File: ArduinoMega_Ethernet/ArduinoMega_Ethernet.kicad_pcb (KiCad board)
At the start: 2 copper layers, 101.6 x 53.3 mm, 113 parts, among them J1 RJ45_Amphenol_RJMG1BD3B8K1ANR, J11 Micro_SD_Card_Det_Hirose_DM3AT, J2 SD_DET_JUMP, J3 IMU_INT1_JUMP, J4 IMU_INT2_JUMP, J5 ETHER_INT_JUMP, J6 RTC_MFP_JUMP, J9 PROGRAM_POWER_USBC, SW1 RST_BTN, U1 ATmega2560-16A, U2 CH340C, U3 ISM330DHCX, U4 W5500, U5 LM3281, U6 74HC244, U7 SE050C2HQ1, U8 AP22804AW5, U9 MCP7940N-xST, Y1 16Mhz, Y2 25Mhz, Y3 Crystal_GND23

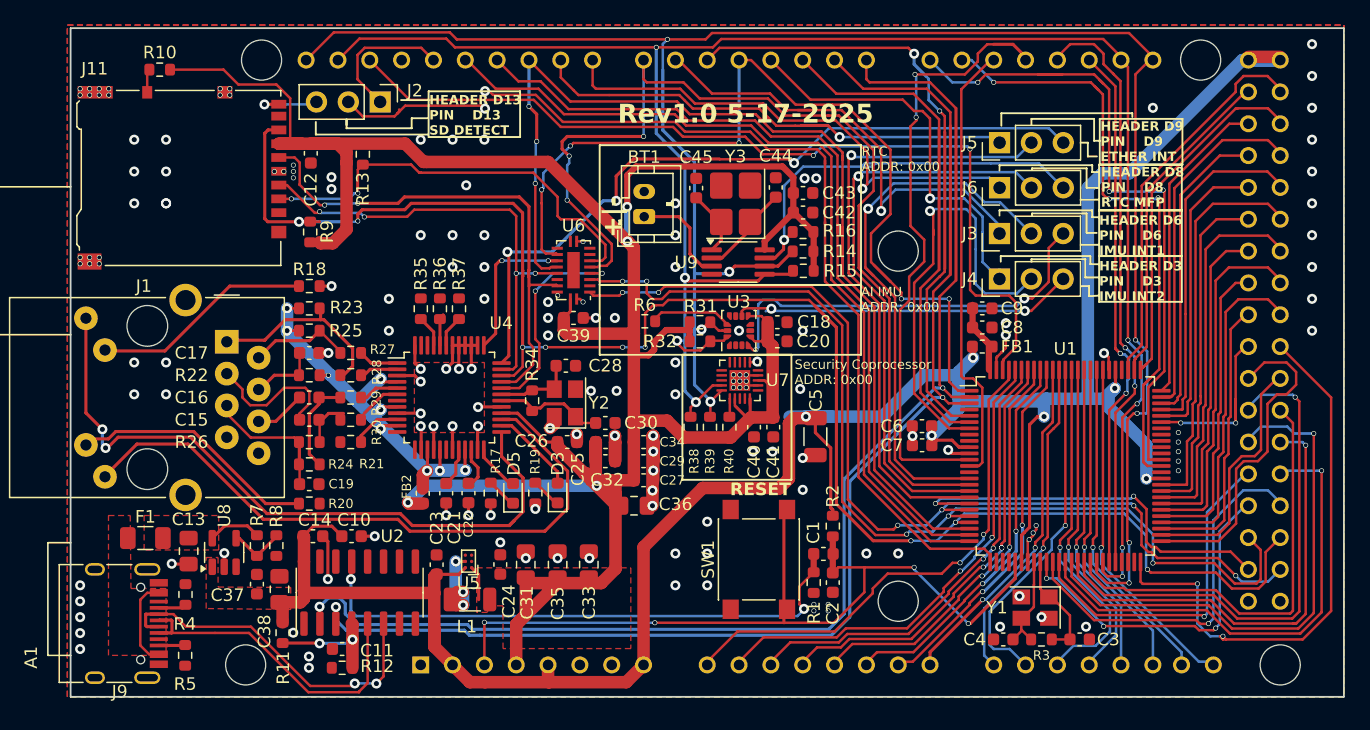
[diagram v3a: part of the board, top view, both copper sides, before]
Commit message: I2C and Silkscreen revision
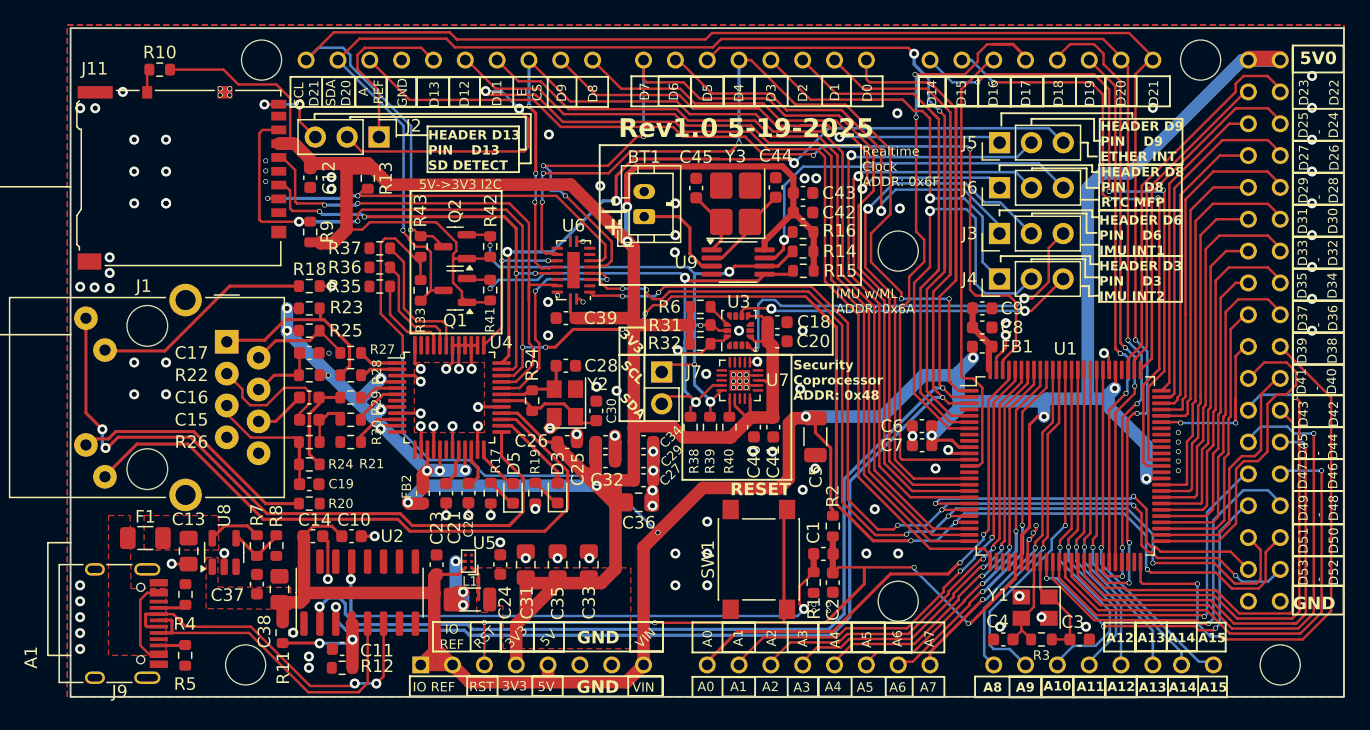
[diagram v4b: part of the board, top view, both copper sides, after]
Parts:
- added J7: EXT_3V3_I2C, Connector_PinHeader_2.54mm:PinHeader_1x02_P2.54mm_Vertical, F.Cu at (90.3, 155.7)
- added Q1: BSS138, Package_TO_SOT_SMD:SOT-23, F.Cu at (73.9, 149.2)
- added Q2: BSS138, Package_TO_SOT_SMD:SOT-23, F.Cu at (73.9, 145.7)
- added R33: 10k, Resistor_SMD:R_0603_1608Metric, F.Cu at (71.1, 149.2)
- added R41: 10k, Resistor_SMD:R_0603_1608Metric, F.Cu at (76.7, 149.2)
- added R42: 10k, Resistor_SMD:R_0603_1608Metric, F.Cu at (76.7, 145.7)
- added R43: 10k, Resistor_SMD:R_0603_1608Metric, F.Cu at (71.1, 145.7)
- moved R37 7.95 mm to (67.8, 145.8), turned to 0 degrees
- moved R36 5.82 mm to (67.8, 147.3), turned to 0 degrees
- moved R6 4.57 mm to (93.4, 150.5)
- moved R35 3.73 mm to (67.8, 148.9), turned to 0 degrees
- moved J2 2.80 mm to (67.8, 136.9)
- moved R13 1.97 mm to (66.9, 140.2)
- moved C12 1.95 mm to (62.3, 140.2)
- moved C30 1.21 mm to (85.1, 158.8), turned to -90 degrees
- moved C39 0.61 mm to (82.7, 151.4), turned to 0 degrees
- moved C36 0.46 mm to (88.5, 166.1)
- moved R31 0.23 mm to (93.4, 151.9)
- moved R32 0.20 mm to (93.4, 153.4)
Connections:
- A1 pad NC: /IOREF0 -> +5V
- R14 pad 2: /PIN_D21 -> /I2C_SCL_3V3
- R15 pad 2: /PIN_D20 -> /I2C_SDA_3V3
- R31 pad 2: /PIN_D21 -> /I2C_SCL_3V3
- R32 pad 2: /PIN_D20 -> /I2C_SDA_3V3
- R38 pad 2: /PIN_D20 -> /I2C_SDA_3V3
- R39 pad 2: /PIN_D21 -> /I2C_SCL_3V3
- U3 pad 13: /PIN_D21 -> /I2C_SCL_3V3
- U3 pad 14: /PIN_D20 -> /I2C_SDA_3V3
- U7 pad 10: /PIN_D21 -> /I2C_SCL_3V3
- U7 pad 9: /PIN_D20 -> /I2C_SDA_3V3
- U9 pad 5: /PIN_D20 -> /I2C_SDA_3V3
- U9 pad 6: /PIN_D21 -> /I2C_SCL_3V3
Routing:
- net /I2C_SDA_3V3: track 0.00 -> 50.7 mm, vias 0 -> 4
- net +5V: track 205.3 -> 254.3 mm, vias 6 -> 8
- net /I2C_SCL_3V3: track 0.00 -> 48.1 mm, vias 0 -> 5
- net /PIN_D20: track 157.6 -> 134.7 mm, vias 8 -> 5
- net +3V3: track 236.2 -> 257.9 mm
- net /PIN_D21: track 162.8 -> 141.1 mm, vias 8 -> 5
- net /PIN_D13: track 82.8 -> 91.4 mm
- net Net-(U4-PMODE2): track 2.52 -> 10.8 mm
- net GND: track 68.0 -> 60.6 mm, vias 162 -> 142
- net Net-(U4-PMODE1): track 2.48 -> 9.25 mm
- net Net-(U4-PMODE0): track 2.52 -> 7.22 mm
- net Net-(U3-CS): track 6.36 -> 1.93 mm
- net /ETHER_CS: track 86.5 -> 82.4 mm
- net /PIN_D50: track 137.2 -> 140.8 mm
- net /HEAD_D13: track 11.2 -> 14.0 mm
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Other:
- board text added: "3V3"
- board text added: "5V"
- board text added: "5V->3V3 I2C"
- board text added: "5V0"
- board text added: "A REF"
- board text added: "A0"
- board text added: "A1"
- board text added: "A10"
- board text added: "A11"
- board text added: "A12"
- board text added: "A13"
- board text added: "A14"
- board text added: "A15"
- board text added: "A2"
- board text added: "A3"
- board text added: "A4"
- board text added: "A5"
- board text added: "A6"
- board text added: "A7"
- board text added: "A8"
- board text added: "A9"
- board text added: "D0"
- board text added: "D1"
- board text added: "D11"
- board text added: "D12"
- board text added: "D13"
- board text added: "D14"
- board text added: "D15"
- board text added: "D16"
- board text added: "D17"
- board text added: "D18"
- board text added: "D19"
- board text added: "D2"
- board text added: "D20"
- board text added: "D21"
- board text added: "D23 D22"
- board text added: "D25 - D24"
- board text added: "D27 D26"
- board text added: "D29 - D28"
- board text added: "D3"
- board text added: "D31 D30"
- board text added: "D33 - D32"
- board text added: "D35 D34"
- board text added: "D37 - D36"
- board text added: "D39 D38"
- board text added: "D4"
- board text added: "D41 - D40"
- board text added: "D43 D42"
- board text added: "D45 - D44"
- board text added: "D47 D46"
- board text added: "D49 - D48"
- board text added: "D5"
- board text added: "D51 D50"
- board text added: "D53 - D52"
- board text added: "D6"
- board text added: "D7"
- board text added: "D8"
- board text added: "D9"
- board text added: "E CS"
- board text added: "GND"
- board text added: "IMU w/ML ADDR: 0x6A"
- board text added: "IO REF"
- board text added: "RST"
- board text added: "Realtime Clock ADDR: 0x6F"
- board text added: "Rev1.0 5-19-2025"
- board text added: "SCL"
- board text added: "SCL D21"
- board text added: "SDA"
- board text added: "SDA D20"
- board text added: "Security Coprocessor ADDR: 0x48"
- board text added: "VIN"
- board text removed: "AI IMU ADDR: 0x00"
- board text removed: "RTC ADDR: 0x00"
- board text removed: "Rev1.0 5-17-2025"
- board text removed: "Security Coprocessor ADDR: 0x00"

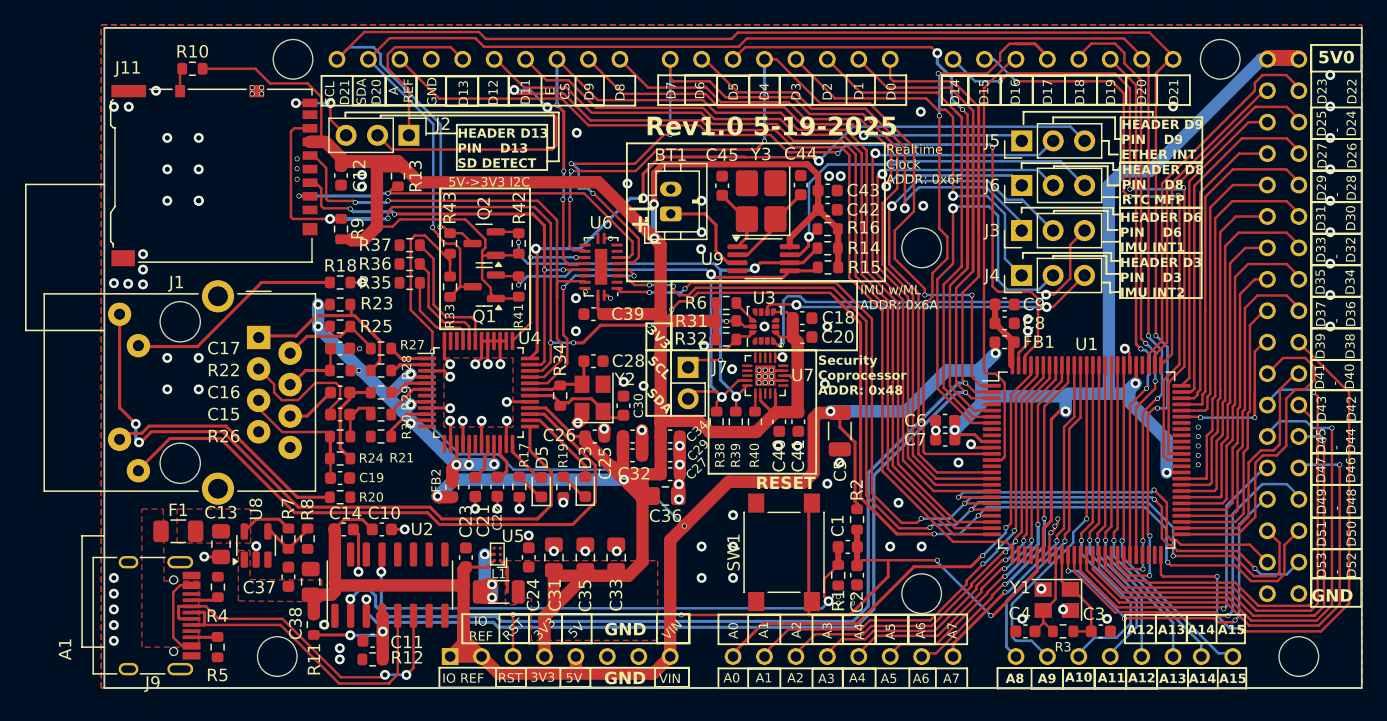
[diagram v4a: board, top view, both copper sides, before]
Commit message: update level shifter, configurable pmode
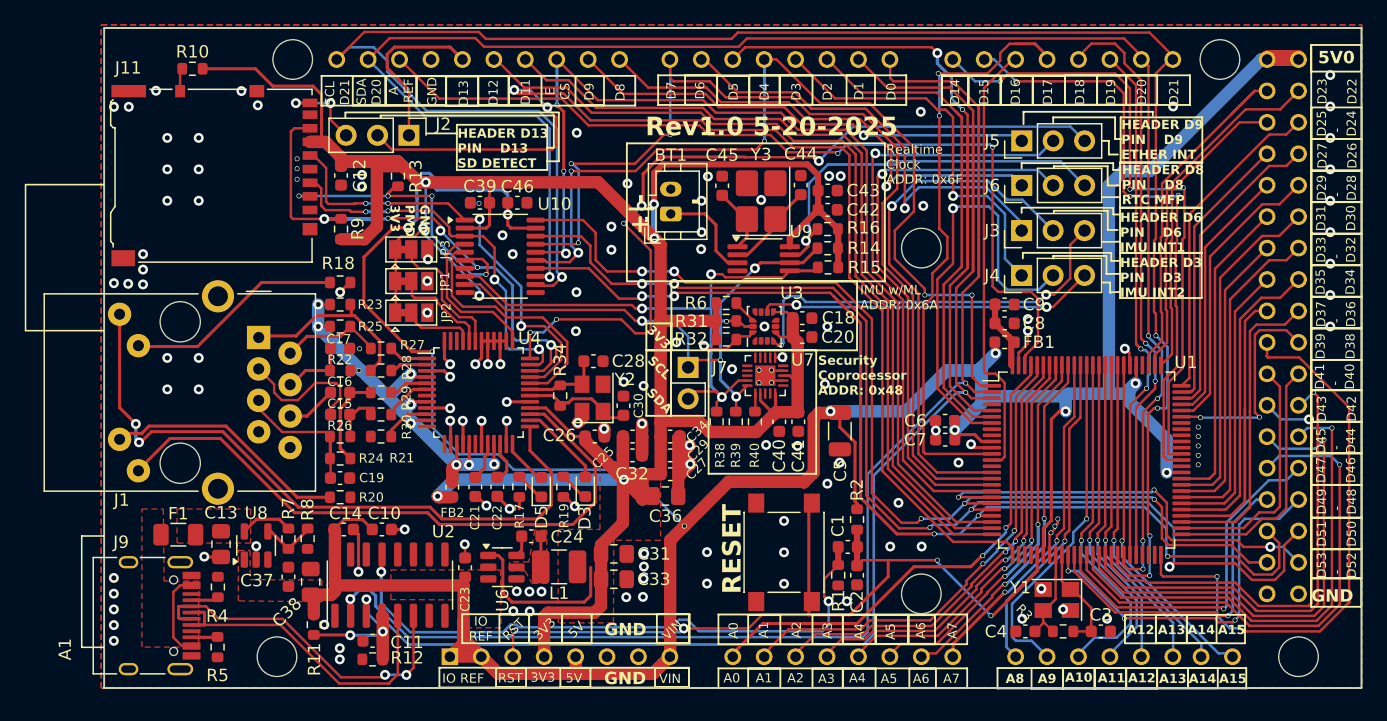
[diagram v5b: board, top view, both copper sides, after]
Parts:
- removed C35: 10uF, Capacitor_SMD:C_0805_2012Metric_Pad1.18x1.45mm_HandSolder
- removed Q1, Q2: BSS138, Package_TO_SOT_SMD:SOT-23
- removed R33, R35, R36, R37, R41, R42, R43: 10k, Resistor_SMD:R_0603_1608Metric
- removed U5: LM3281, Package_BGA:Texas_DSBGA-6_0.9x1.4mm_Layout2x3_P0.5mm
- added C46: 1uF, Capacitor_SMD:C_0603_1608Metric, F.Cu at (76.5, 142.4)
- added JP1: PMODE1, Jumper:SolderJumper-3_P1.3mm_Bridged12_Pad1.0x1.5mm, F.Cu at (68.0, 148.7)
- added JP2: PMODE0, Jumper:SolderJumper-3_P1.3mm_Bridged12_Pad1.0x1.5mm, F.Cu at (68.0, 151.3)
- added JP3: PMODE2, Jumper:SolderJumper-3_P1.3mm_Bridged12_Pad1.0x1.5mm, F.Cu at (68.0, 146.2)
- added U10: TXS0108EPW, Package_SO:TSSOP-20_4.4x6.5mm_P0.65mm, F.Cu at (75.2, 146.7)
- A1: footprint footprints:ARDUINO_A000067 -> CUSTOM_PAD:ARDUINO_A000067
- C20, C34, C39, C41, C43, C6: value 100nF -> 1uF
- C23: value 2.2uF -> 10uF
- C24: value 2.2uF -> 100nF
- C3, C4: value Var -> 22pF
- C31, C33: value 10uF -> 22uF
- L1: value 0.47uH/2A -> 4.7uH; footprint Inductor_SMD:L_1206_3216Metric -> Inductor_SMD:L_1210_3225Metric_Pad1.42x2.65mm_HandSolder
- U6: value 74HC244 -> AP63203WU; footprint Package_DFN_QFN:WQFN-20-1EP_2.5x4.5mm_P0.5mm_EP1x2.9mm -> Package_TO_SOT_SMD:TSOT-23-6
- moved U6 25.6 mm to (75.3, 171.8), turned to 0 degrees
- moved C39 12.9 mm to (73.5, 142.4)
- moved L1 5.28 mm to (79.9, 171.8)
- moved C31 4.86 mm to (84.3, 170.8), turned to 0 degrees
- moved C33 1.77 mm to (84.3, 172.8), turned to 0 degrees
- moved C24 1.72 mm to (77.7, 169.3), turned to 180 degrees
- moved C23 0.81 mm to (72.3, 171.9)
- moved F1 0.28 mm to (49.1, 169.2)
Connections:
- net /I2C_SCL_3V3 renamed /PWRandPRG/IMU_SCL
- net /I2C_SDA_3V3 renamed /PWRandPRG/IMU_SDA
- A1 pad 22: /PIN_D23 -> /PIN_D22
- A1 pad 23: /PIN_D22 -> /PIN_D23
- A1 pad 24: /PIN_D25 -> /PIN_D24
- A1 pad 25: /PIN_D24 -> /PIN_D25
- A1 pad 26: /PIN_D27 -> /PIN_D26
- A1 pad 27: /PIN_D26 -> /PIN_D27
- A1 pad 28: /PIN_D29 -> /PIN_D28
- A1 pad 29: /PIN_D28 -> /PIN_D29
- A1 pad 30: /PIN_D31 -> /PIN_D30
- A1 pad 31: /PIN_D30 -> /PIN_D31
- A1 pad 32: /PIN_D33 -> /PIN_D32
- A1 pad 33: /PIN_D32 -> /PIN_D33
- A1 pad 34: /PIN_D35 -> /PIN_D34
- A1 pad 35: /PIN_D34 -> /PIN_D35
- A1 pad 36: /PIN_D37 -> /PIN_D36
- A1 pad 37: /PIN_D36 -> /PIN_D37
- A1 pad 38: /PIN_D39 -> /PIN_D38
- A1 pad 39: /PIN_D38 -> /PIN_D39
- A1 pad 40: /PIN_D41 -> /PIN_D40
- A1 pad 41: /PIN_D40 -> /PIN_D41
- A1 pad 42: /PIN_D43 -> /PIN_D42
- A1 pad 43: /PIN_D42 -> /PIN_D43
- A1 pad 44: /PIN_D45 -> /PIN_D44
- A1 pad 45: /PIN_D44 -> /PIN_D45
- A1 pad 46: /PIN_D47 -> /PIN_D46
- A1 pad 47: /PIN_D46 -> /PIN_D47
- A1 pad 48: /PIN_D49 -> /PIN_D48
- A1 pad 49: /PIN_D48 -> /PIN_D49
- A1 pad 50: /PIN_D51 -> /PIN_D50
- A1 pad 51: /PIN_D50 -> /PIN_D51
- A1 pad 52: /PIN_D53 -> /PIN_D52
- A1 pad 53: /PIN_D52 -> /PIN_D53
- C24 pad 1: +3V3 -> Net-(U6-SW)
- C24 pad 2: GND -> Net-(U6-BST)
- J11 pad 7: /PIN_D50 -> /PWRandPRG/ETHERNET_MISO
- L1 pad 1: Net-(U5-SW) -> Net-(U6-SW)
- R9 pad 2: /PIN_D50 -> /PWRandPRG/ETHERNET_MISO
- U4 pad 34: /PIN_D50 -> /PWRandPRG/ETHERNET_MISO
- U6 pad 1: GND -> +3V3
- U6 pad 2: /PIN_D52 -> +5V
- U6 pad 3: unconnected-(U6-2Y0-Pad3) -> +5V
- U6 pad 4: /PIN_D51 -> GND
- U6 pad 5: /PWRandPRG/ETHERNET_CS -> Net-(U6-SW)
- U6 pad 6: /ETHER_~{RST} -> Net-(U6-BST)
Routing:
- net /PIN_D50: track 140.8 -> 90.3 mm, vias 9 -> 5
- net /PWRandPRG/ETHERNET_MISO: track 0.00 -> 49.1 mm, vias 0 -> 5
- net +5V: track 254.3 -> 272.2 mm, vias 8 -> 10
- net /PIN_D21: track 141.1 -> 153.9 mm
- net /PIN_D51: track 81.1 -> 91.5 mm
- net +3V3: track 257.9 -> 268.1 mm, vias 4 -> 7
- net GND: track 60.6 -> 70.2 mm, vias 142 -> 143
- net /PWRandPRG/SDCARD_CS: track 33.0 -> 24.7 mm, vias 2 -> 4
- net Net-(U5-SW): track 8.03 -> 0.00 mm, vias 3 -> 0
- net /PIN_D28: track 27.4 -> 21.1 mm
- net /PIN_D52: track 79.3 -> 85.5 mm, vias 6 -> 5
- net /PWRandPRG/ETHERNET_SCLK: track 41.8 -> 35.8 mm, vias 2 -> 4
- net /PIN_D41: track 26.4 -> 20.6 mm
- net /PIN_D30: track 31.1 -> 25.4 mm
- net /ETHER_~{INT}: track 59.5 -> 65.1 mm, vias 3 -> 5
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- added copper zone on F.Cu, net Net-(U6-SW)
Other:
- board text added: "GND PMD 3V3"
- board text added: "Rev1.0 5-20-2025"
- board text removed: "5V->3V3 I2C"
- board text removed: "Rev1.0 5-19-2025"

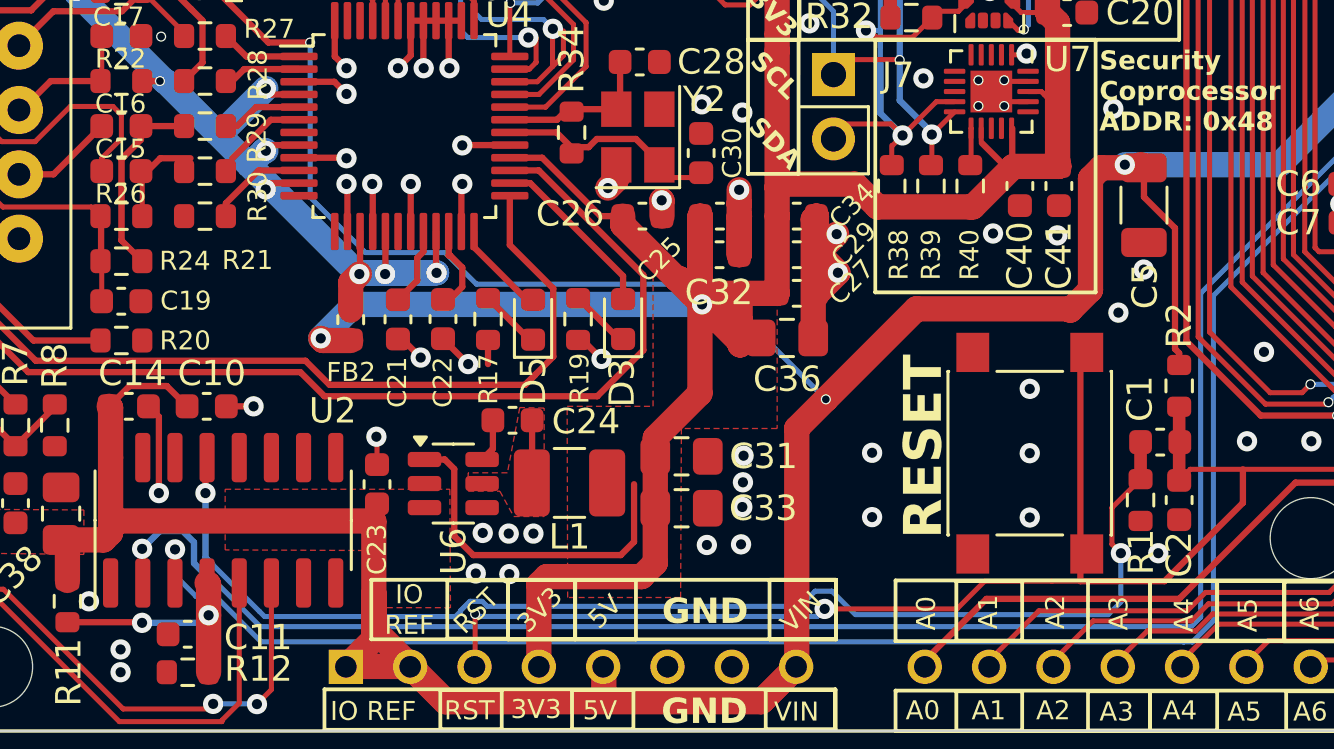
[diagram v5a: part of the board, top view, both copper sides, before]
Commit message: Add files via upload
fix undersized capacitors
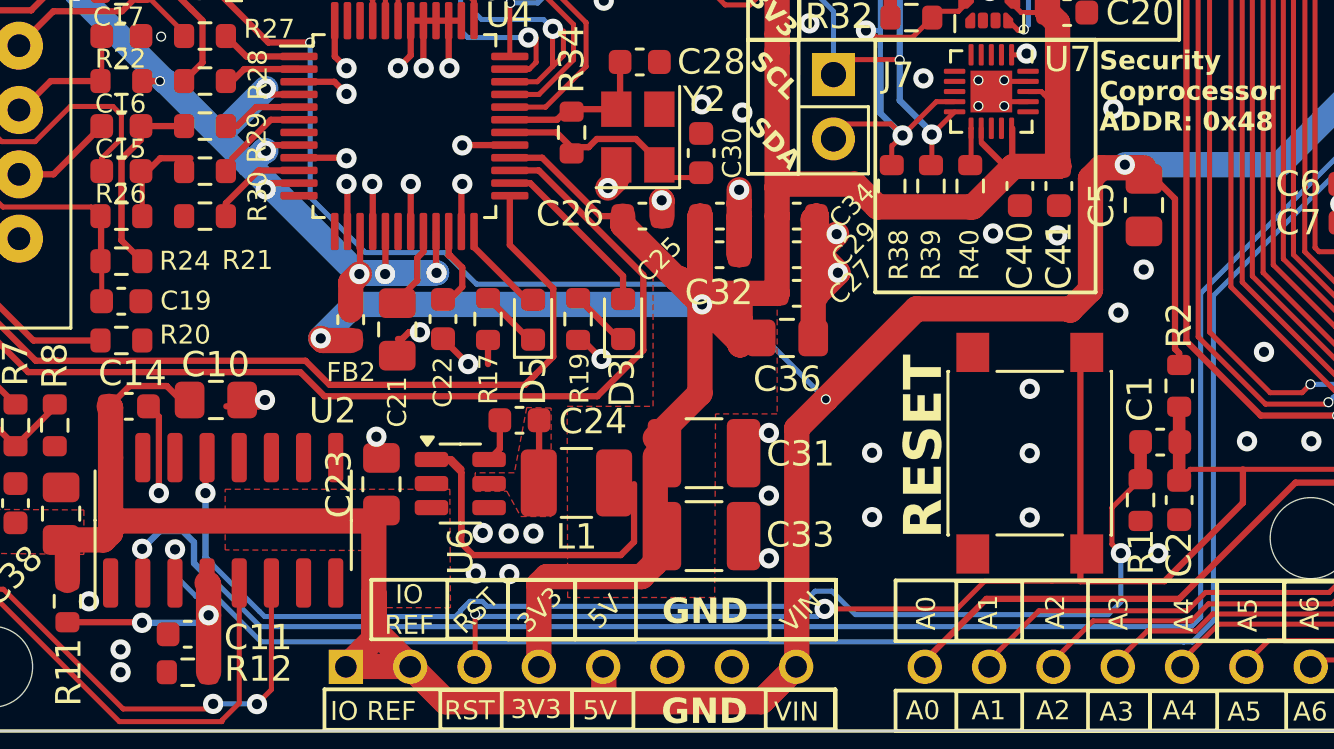
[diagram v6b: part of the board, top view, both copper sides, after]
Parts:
- C10, C21, C23: footprint Capacitor_SMD:C_0603_1608Metric -> Capacitor_SMD:C_0805_2012Metric_Pad1.18x1.45mm_HandSolder
- C31, C33: footprint Capacitor_SMD:C_0805_2012Metric_Pad1.18x1.45mm_HandSolder -> Capacitor_SMD:C_1210_3225Metric_Pad1.33x2.70mm_HandSolder
- C5: footprint Capacitor_SMD:C_1206_3216Metric -> Capacitor_SMD:C_0805_2012Metric_Pad1.18x1.45mm_HandSolder
- Y3: value Crystal_GND23 -> 32.768kHz
- moved C33 1.41 mm to (85.2, 173.9)
- moved C31 0.90 mm to (85.2, 170.7)
- moved C10 0.44 mm to (66.0, 168.6)
- moved C21 0.40 mm to (73.1, 165.8)
- moved C24 0.28 mm to (78.0, 169.3)
- moved L1 0.28 mm to (80.2, 171.8)
- moved U6 0.27 mm to (75.6, 171.8)
- moved C23 0.17 mm to (72.5, 171.9)
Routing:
- net +3V3: track 268.1 -> 271.9 mm
- net GND: track 70.2 -> 70.6 mm, vias 143 -> 141
